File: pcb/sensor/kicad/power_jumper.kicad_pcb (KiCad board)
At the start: 2 copper layers, 177.1 x 37.6 mm, 5 parts, among them J1 FPC 6P 0.5 mm

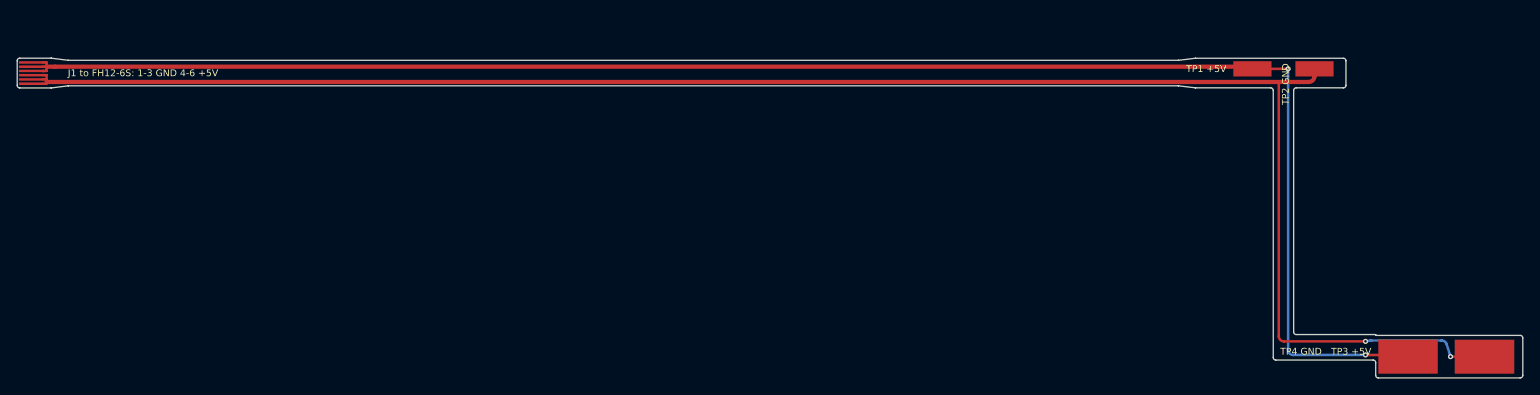
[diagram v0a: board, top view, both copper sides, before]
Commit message: Smaller plate, flex ramps and tape points, battery-free tongue on the sensor flex, back cover hooks
- Plate 72 x 132, 5 V contact in the corner, band groove, microphone below the band, two-layer
  sensor flex (D-47)
- Ramps over the flex slopes; tape geometry and tape renders (render_tape.py, D-48)
- Battery-free tongue moved from the 5 V jumper to the sensor flex: under the trim's tab and strip,
  under the floor insert, which hangs from the strip; EU tongue under its floor insert (D-49)
- Back cover: bottom latch 2.9 mm from the edge, end-section snap hooks, notch for the run under
  the GND block; plate clips kept for PETG
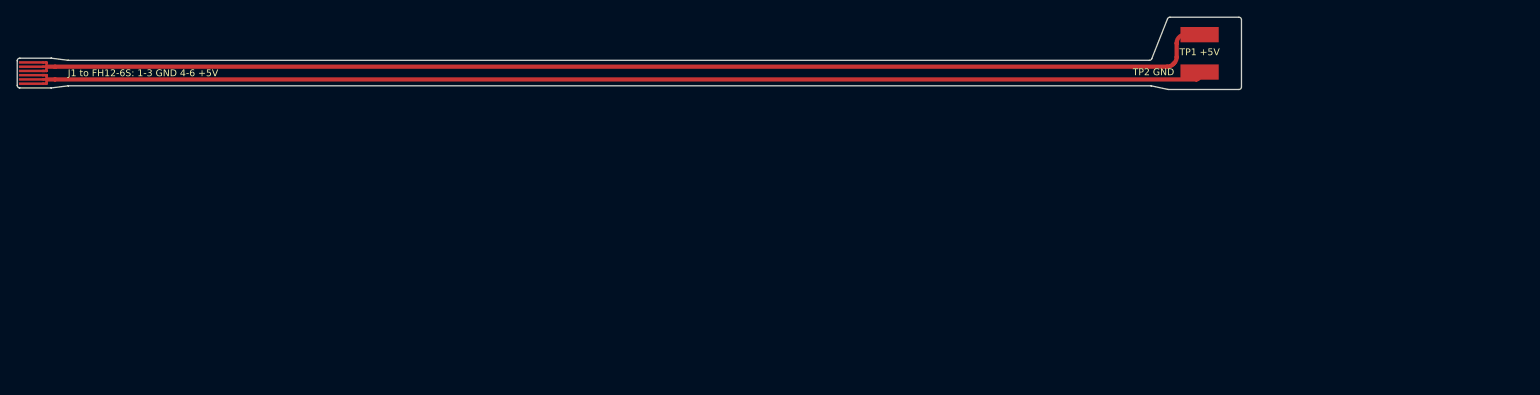
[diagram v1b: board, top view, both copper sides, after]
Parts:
- removed TP3: +5V floor pad, sensor:Contact_Pad_7x4mm
- removed TP4: GND floor pad, sensor:Contact_Pad_7x4mm
- moved TP2 13.5 mm to (239.1, 99.9)
- moved TP1 7.40 mm to (239.1, 95.5)
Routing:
- net GND: track 208.4 -> 138.7 mm, vias 2 -> 0
- net +5V: track 192.4 -> 140.8 mm, vias 2 -> 0
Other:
- board size 177.1 x 37.6 mm -> 144 x 8.5 mm
- board text added: "Flat length 144.0 mm incl. 40 mm service loop (Z-fold)"
- board text removed: "Flat length 156.3 mm incl. 40 mm service loop (Z-fold)"
- board text removed: "TP3 +5V"
- board text removed: "TP4 GND"
